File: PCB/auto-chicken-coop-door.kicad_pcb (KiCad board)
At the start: 2 copper layers, 85.1 x 45.1 mm, 17 parts, among them J10 Charger, J11 Charger, J2 Conn_Left, J3 Conn_Middle, J4 Conn_Right, J8 Conn_01x01, J9 BuckBoost, M1 Motor_DC, Q1 TIP122, U1 Arduino_Pro_Mini, U2 DS3231, U3 Sparkfun_Dual_Motor_Driver_TB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, U4 SSD1306_OLED_128x32

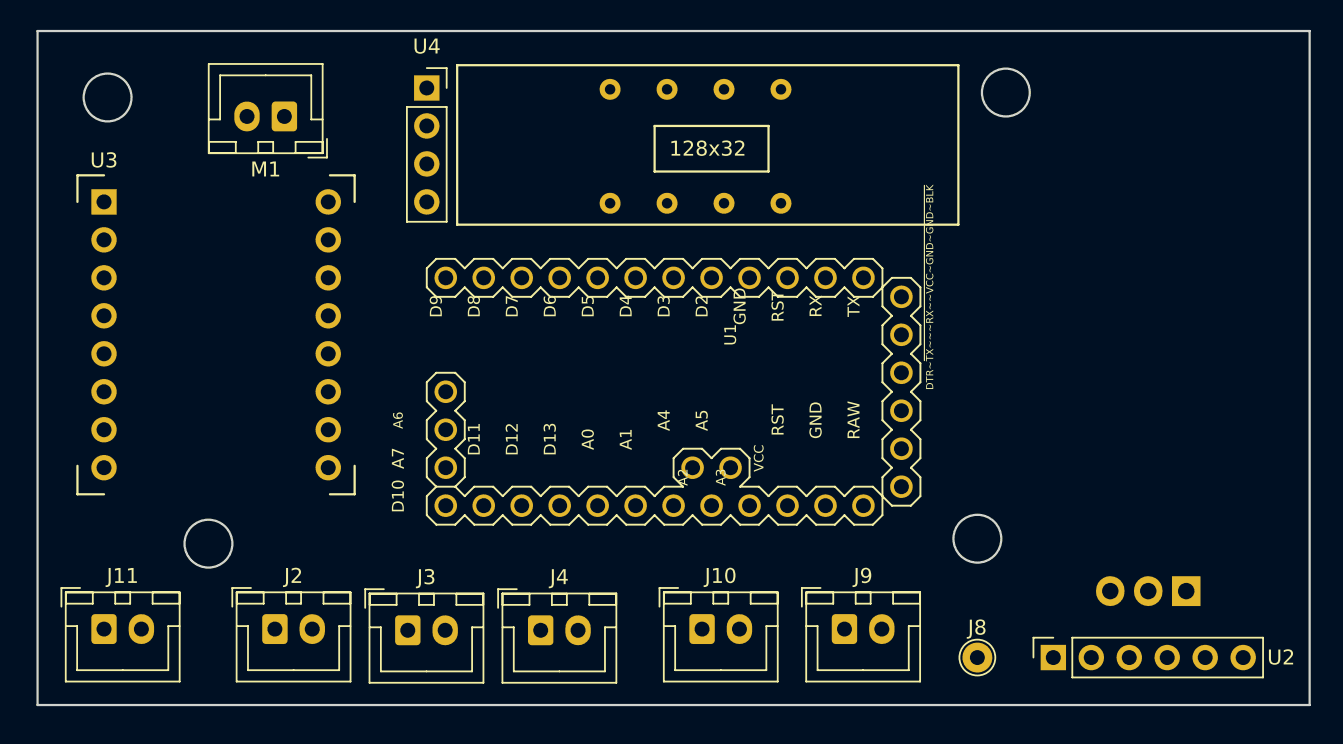
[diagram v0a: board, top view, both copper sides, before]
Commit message: PCB layout complete
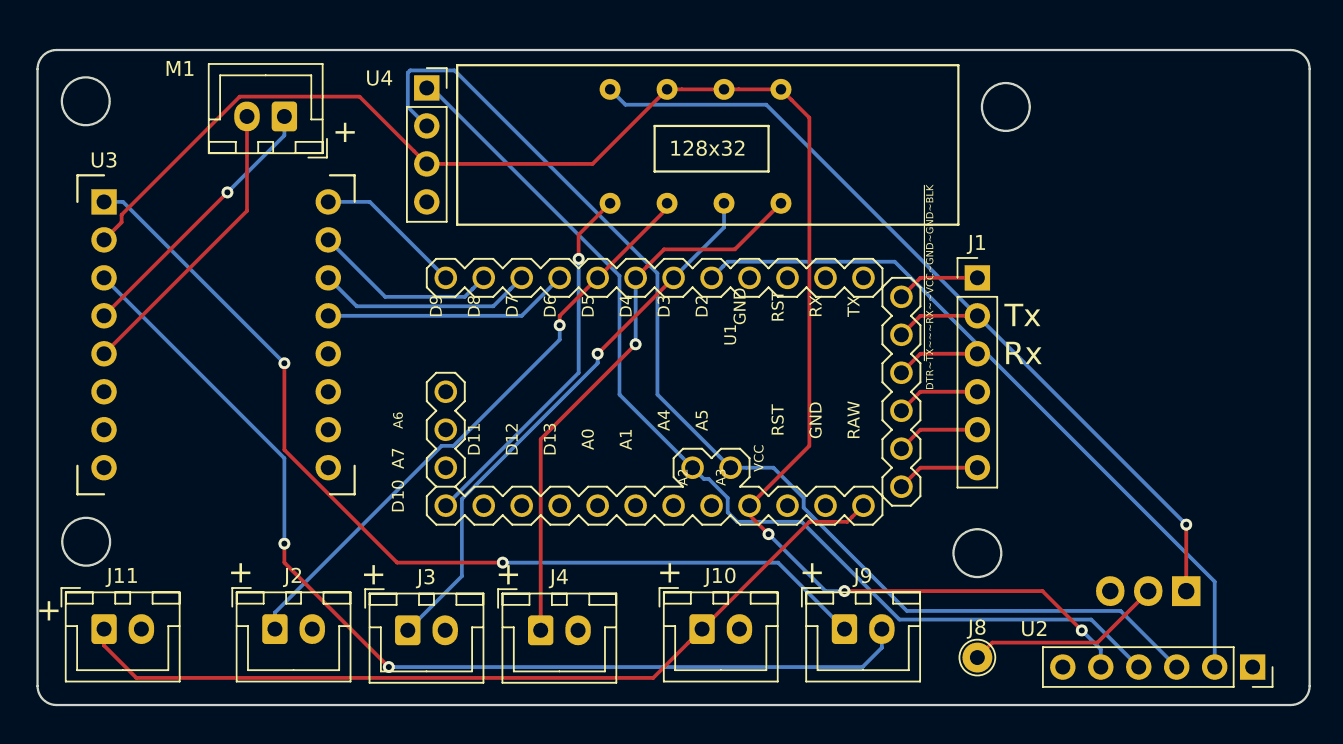
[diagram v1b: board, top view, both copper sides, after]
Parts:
- added J1: Programming_Headers, Connector_PinHeader_2.54mm:PinHeader_1x06_P2.54mm_Vertical, F.Cu at (194.9, 90.2)
- moved U2 13.4 mm to (213.4, 116.2), turned to 270 degrees
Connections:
- U1 pad RX@1: (no net) -> Net-(J1-Pad3)
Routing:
- net VCC: track 0.00 -> 112.8 mm, vias 0 -> 3
- net SCL: track 0.00 -> 77.2 mm
- net SDA: track 0.00 -> 68.9 mm
- net Net-(J9-Pad2): track 0.00 -> 68.7 mm, vias 0 -> 2
- net Net-(J9-Pad1): track 0.00 -> 64.8 mm, vias 0 -> 2
- net Net-(J10-Pad1): track 0.00 -> 57.6 mm
- net Net-(Q1-Pad1): track 0.00 -> 55.0 mm, vias 0 -> 1
- net Net-(U1-PadD2): track 0.00 -> 48.7 mm
- net D5: track 0.00 -> 39.8 mm, vias 0 -> 1
- net D4: track 0.00 -> 38.0 mm, vias 0 -> 1
- net D3: track 0.00 -> 37.3 mm, vias 0 -> 1
- net D10: track 0.00 -> 24.8 mm, vias 0 -> 1
- net Net-(M1-Pad2): track 0.00 -> 19.8 mm
- net Net-(M1-Pad1): track 0.00 -> 18.3 mm, vias 0 -> 1
- net Net-(U1-PadD6): track 0.00 -> 16.5 mm
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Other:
- board size 85.1 x 45.1 mm -> 85.1 x 43.8 mm
- board text added: "+"
- board text added: "Chicken Guard V1.0 J.Lam - 2020/05/13"
- board text added: "Rx"
- board text added: "Tx"

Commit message: Add silkscreen labels
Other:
- board text added: "BuckIn"
- board text added: "BuckOut"
- board text added: "Left"
- board text added: "Middle"
- board text added: "Right"
- board text added: "Solar"
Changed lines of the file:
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@@
   (general
     (thickness 1.6)
-    (drawings 26)
+    (drawings 32)
     (tracks 159)
     (zones 0)
@@
       (outputformat 1)
       (mirror false)
-      (drillshape 1)
+      (drillshape 0)
       (scaleselection 1)
-      (outputdirectory ""))
+      (outputdirectory "plots/"))
   )
   (net 0 "")
@@
     (descr "JST XH series connector, B02B-XH-A (http://www.jst-mfg.com/product/pdf/eng/eXH.pdf), generated with kicad-footprint-generator")
     (tags "connector JST XH side entry")
-    (fp_text reference J11 (at 1.25 -3.55) (layer F.SilkS)
+    (fp_text reference J11 (at 2.413 -3.556) (layer F.SilkS)
       (effects (font (size 1 1) (thickness 0.15)))
     )
@@
       (net 46 "Net-(J1-Pad6)"))
   )
+  (gr_text BuckOut (at 187.198 108.331) (layer F.SilkS)
+    (effects (font (size 1.2 1.2) (thickness 0.2)))
+  )
+  (gr_text BuckIn (at 177.546 108.204) (layer F.SilkS)
+    (effects (font (size 1.2 1.2) (thickness 0.2)))
+  )
+  (gr_text Solar (at 140.589 108.331) (layer F.SilkS)
+    (effects (font (size 1.2 1.2) (thickness 0.2)))
+  )
+  (gr_text Right (at 167.132 108.204) (layer F.SilkS)
+    (effects (font (size 1.2 1.2) (thickness 0.2)))
+  )
+  (gr_text Middle (at 158.115 108.204) (layer F.SilkS)
+    (effects (font (size 1.2 1.2) (thickness 0.2)))
+  )
+  (gr_text Left (at 149.225 108.331) (layer F.SilkS)
+    (effects (font (size 1.2 1.2) (thickness 0.2)))
+  )
   (gr_text "Chicken Guard V1.0\nJ.Lam - 2020/05/13" (at 175.006 97.917) (layer B.SilkS)

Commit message: Add ground plane
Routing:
- added copper zone on F.Cu, net GND
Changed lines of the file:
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@@
     (effects (font (size 1.5 1.5) (thickness 0.3)))
   )
-  (gr_circle (center 194.945 108.585) (end 196.536305 108.585) (layer F.Mask) (width 2))
-  (gr_circle (center 196.85 78.74) (end 198.441305 78.74) (layer F.Mask) (width 2))
-  (gr_circle (center 135.441695 107.95) (end 137.033 107.95) (layer F.Mask) (width 2))
-  (gr_circle (center 135.306 78.359) (end 136.897305 78.359) (layer F.Mask) (width 2))
+  (gr_circle (center 194.945 108.585) (end 196.536305 108.585) (layer F.Mask) (width 1.1))
+  (gr_circle (center 196.85 78.74) (end 198.441305 78.74) (layer F.Mask) (width 1.1))
+  (gr_circle (center 135.331 107.823) (end 136.922305 107.823) (layer F.Mask) (width 1.1))
+  (gr_circle (center 135.306 78.359) (end 136.897305 78.359) (layer F.Mask) (width 1.1))
   (gr_circle (center 135.306 78.359) (end 136.906 78.359) (layer Edge.Cuts) (width 0.15))
   (gr_arc (start 215.9 117.475) (end 215.9 118.745) (angle -90) (layer Edge.Cuts) (width 0.15))
@@
   (segment (start 191.135 95.25) (end 189.865 96.52) (width 0.25) (layer F.Cu) (net 47))
   (segment (start 194.945 95.25) (end 191.135 95.25) (width 0.25) (layer F.Cu) (net 47))
+  (zone (net 2) (net_name GND) (layer F.Cu) (hatch edge 0.508)
+    (connect_pads (clearance 0.508))
+    (min_thickness 0.254)
+    (fill yes (arc_segments 16) (thermal_gap 0.508) (thermal_bridge_width 0.508))
+    (polygon
+      (pts
+        (xy 132.08 74.676) (xy 217.424 74.676) (xy 217.424 119.38) (xy 132.08 119.38)
+      )
+    )
+  )
 )

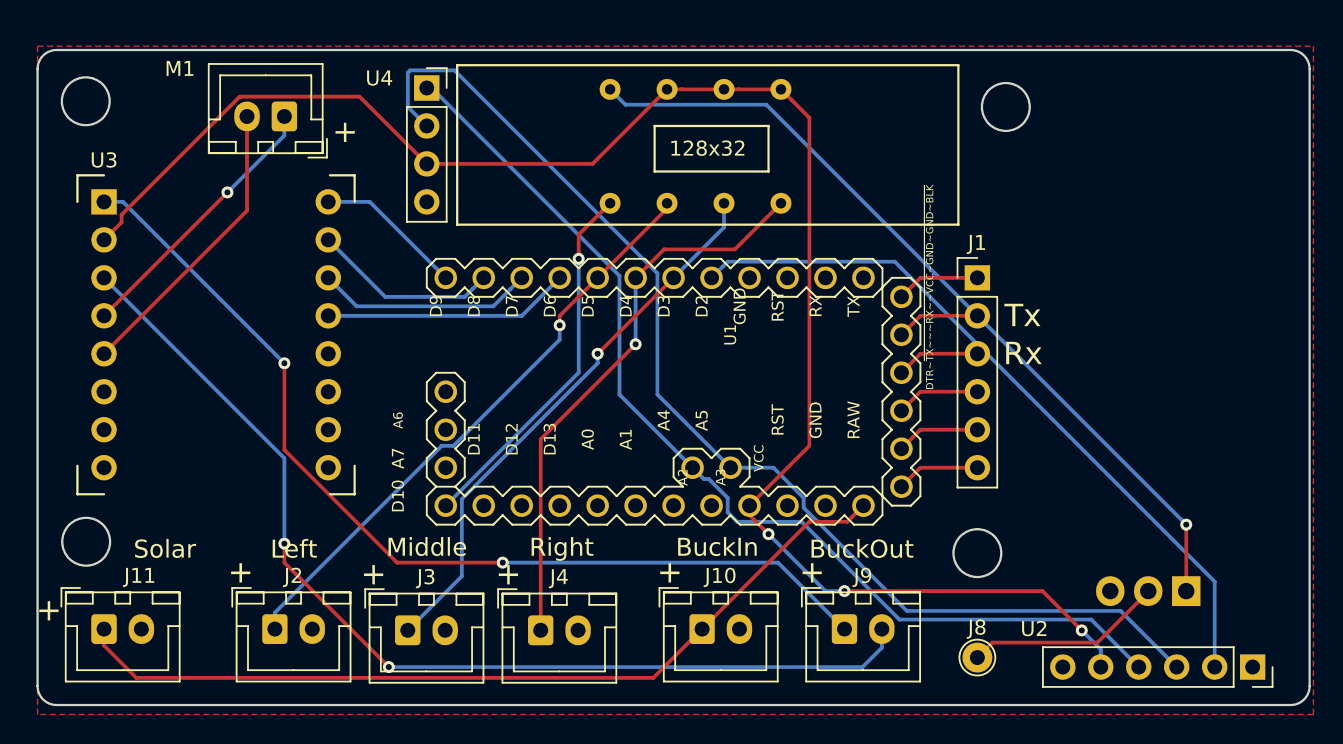
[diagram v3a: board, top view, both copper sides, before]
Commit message: Fix overlapping traces with pad
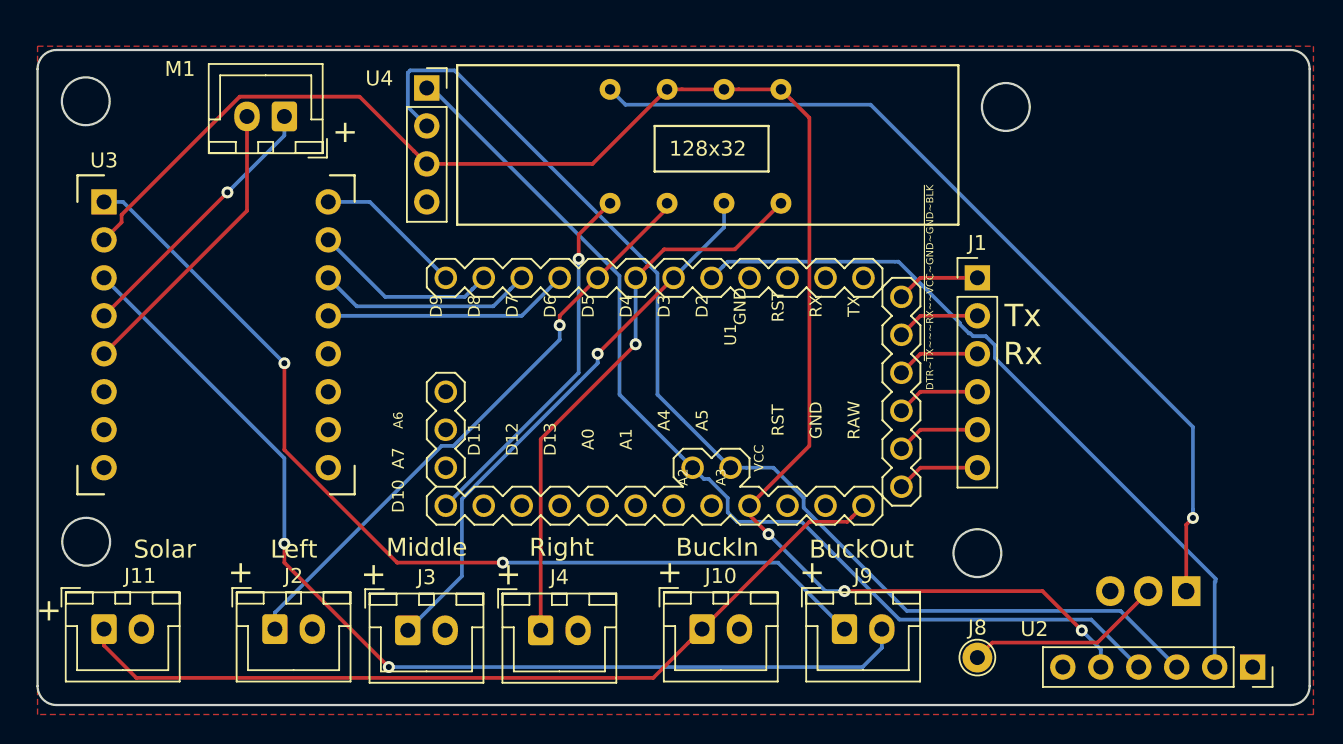
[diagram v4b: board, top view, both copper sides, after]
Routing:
- net Net-(Q1-Pad1): track 55.0 -> 59.5 mm
- net Net-(U1-PadD2): track 48.7 -> 49.3 mm
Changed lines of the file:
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@@
     (thickness 1.6)
     (drawings 32)
-    (tracks 159)
+    (tracks 172)
     (zones 0)
     (modules 18)
@@
   (page A4)
   (layers
-    (0 F.Cu signal)
+    (0 F.Cu signal hide)
     (31 B.Cu signal)
     (32 B.Adhes user)
@@
   (gr_line (start 132.08 76.2) (end 132.08 117.475) (layer Edge.Cuts) (width 0.15))
   (gr_line (start 133.35 74.93) (end 215.9 74.93) (layer Edge.Cuts) (width 0.15))
-  (segment (start 180.822342 78.587342) (end 208.915 106.68) (width 0.25) (layer B.Cu) (net 1))
   (segment (start 170.377831 77.562341) (end 171.402832 78.587342) (width 0.25) (layer B.Cu) (net 1))
-  (via (at 208.915 106.68) (size 0.8) (drill 0.4) (layers F.Cu B.Cu) (net 1))
-  (segment (start 171.402832 78.587342) (end 180.822342 78.587342) (width 0.25) (layer B.Cu) (net 1))
-  (segment (start 208.915 106.68) (end 208.915 111.125) (width 0.25) (layer F.Cu) (net 1))
+  (via (at 209.36416 106.23084) (size 0.8) (drill 0.4) (layers F.Cu B.Cu) (net 1))
+  (segment (start 208.915 106.68) (end 209.36416 106.23084) (width 0.25) (layer F.Cu) (net 1))
+  (segment (start 187.807342 78.587342) (end 209.36416 100.14416) (width 0.25) (layer B.Cu) (net 1))
+  (segment (start 208.915 111.125) (end 208.915 106.68) (width 0.25) (layer F.Cu) (net 1))
+  (segment (start 209.36416 100.14416) (end 209.36416 105.665155) (width 0.25) (layer B.Cu) (net 1))
+  (segment (start 209.36416 105.665155) (end 209.36416 106.23084) (width 0.25) (layer B.Cu) (net 1))
+  (segment (start 171.402832 78.587342) (end 187.807342 78.587342) (width 0.25) (layer B.Cu) (net 1))
   (segment (start 153.61499 78.04999) (end 157.265001 81.700001) (width 0.25) (layer F.Cu) (net 4))
   (segment (start 145.603295 78.04999) (end 153.61499 78.04999) (width 0.25) (layer F.Cu) (net 4))
@@
   (segment (start 178.244001 89.090999) (end 177.918999 89.416001) (width 0.25) (layer B.Cu) (net 39))
   (segment (start 189.418501 89.090999) (end 178.244001 89.090999) (width 0.25) (layer B.Cu) (net 39))
-  (segment (start 210.82 110.492498) (end 189.418501 89.090999) (width 0.25) (layer B.Cu) (net 39))
   (segment (start 210.82 116.205) (end 210.82 110.492498) (width 0.25) (layer B.Cu) (net 39))
+  (segment (start 193.769999 93.274001) (end 193.769999 93.185999) (width 0.25) (layer B.Cu) (net 39))
+  (segment (start 210.885499 110.301499) (end 196.120001 95.536001) (width 0.25) (layer B.Cu) (net 39))
+  (segment (start 189.674999 89.090999) (end 189.484 89.090999) (width 0.25) (layer B.Cu) (net 39))
+  (segment (start 194.380999 93.885001) (end 193.769999 93.274001) (width 0.25) (layer B.Cu) (net 39))
+  (segment (start 194.658999 94.074999) (end 194.469001 93.885001) (width 0.25) (layer B.Cu) (net 39))
+  (segment (start 193.769999 93.185999) (end 189.674999 89.090999) (width 0.25) (layer B.Cu) (net 39))
+  (segment (start 210.885499 110.492498) (end 210.885499 110.301499) (width 0.25) (layer B.Cu) (net 39))
+  (segment (start 194.469001 93.885001) (end 194.380999 93.885001) (width 0.25) (layer B.Cu) (net 39))
+  (segment (start 196.120001 95.536001) (end 196.120001 94.685999) (width 0.25) (layer B.Cu) (net 39))
+  (segment (start 196.120001 94.685999) (end 195.509001 94.074999) (width 0.25) (layer B.Cu) (net 39))
+  (segment (start 195.509001 94.074999) (end 194.658999 94.074999) (width 0.25) (layer B.Cu) (net 39))
   (segment (start 191.135 102.87) (end 189.865 104.14) (width 0.25) (layer F.Cu) (net 46))
   (segment (start 194.945 102.87) (end 191.135 102.87) (width 0.25) (layer F.Cu) (net 46))
